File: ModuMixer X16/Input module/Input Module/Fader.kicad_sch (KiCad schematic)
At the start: 9 parts, among them J5 Screw_Terminal_01x02, J6 Screw_Terminal_01x03, U8 DRV8833PWP

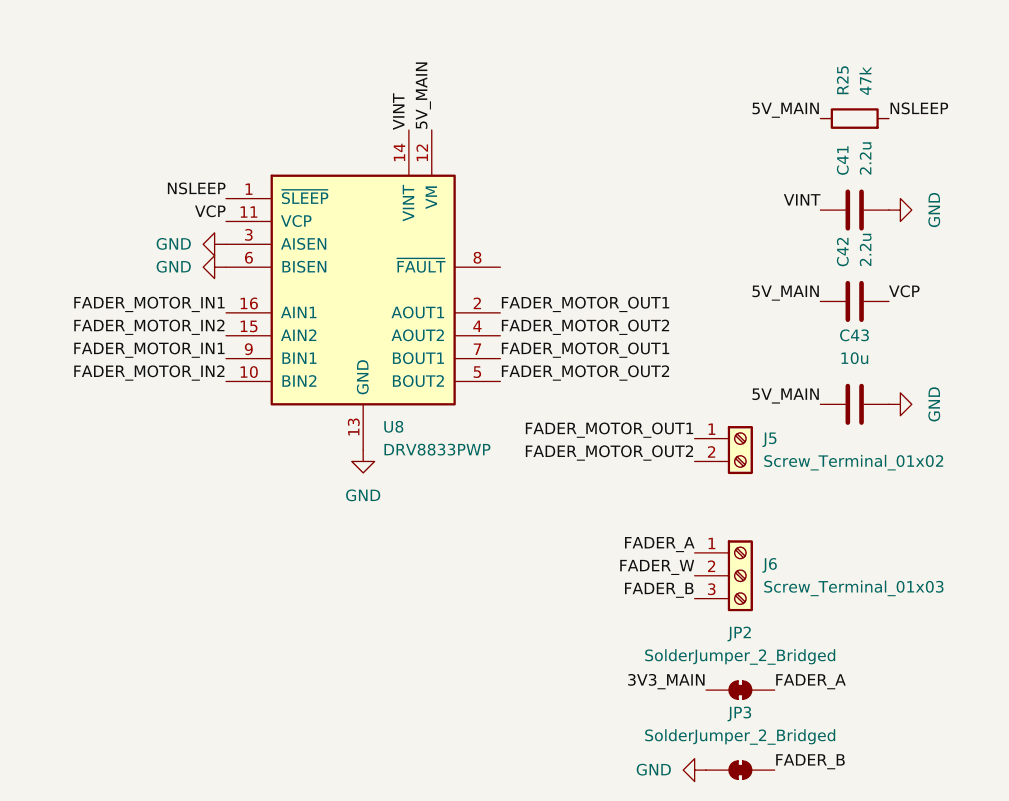
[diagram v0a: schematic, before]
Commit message: MCU replacement finished
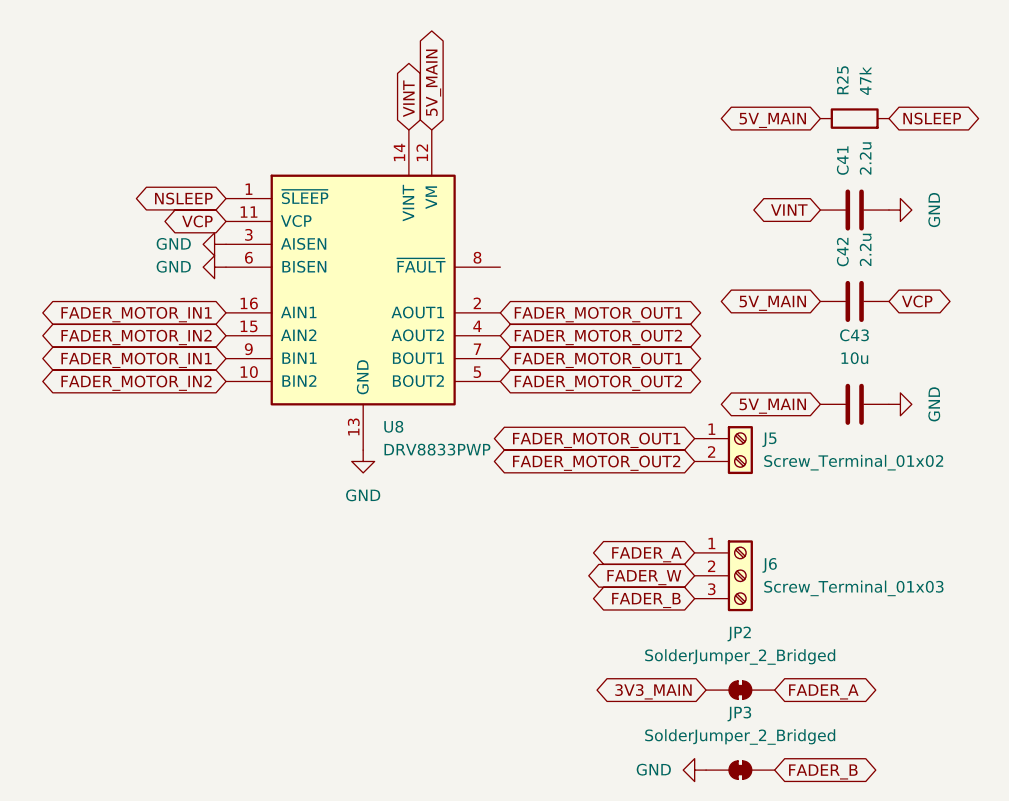
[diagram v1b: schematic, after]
